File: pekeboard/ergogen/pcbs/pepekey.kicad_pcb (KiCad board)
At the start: 2 copper layers, 150.9 x 124.7 mm, 63 parts

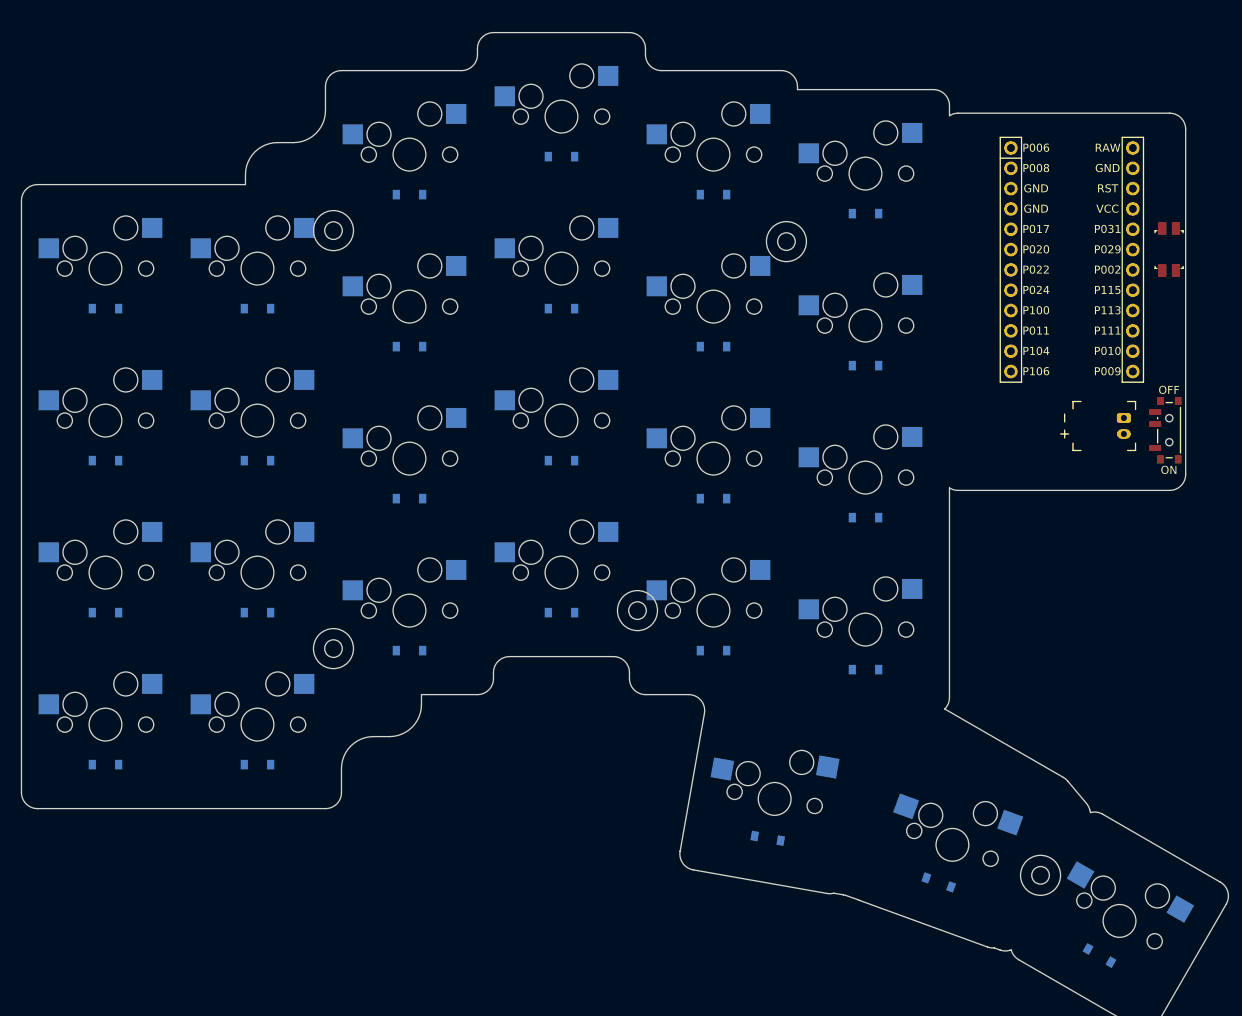
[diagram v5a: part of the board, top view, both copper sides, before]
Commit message: Adjusting mounting holes
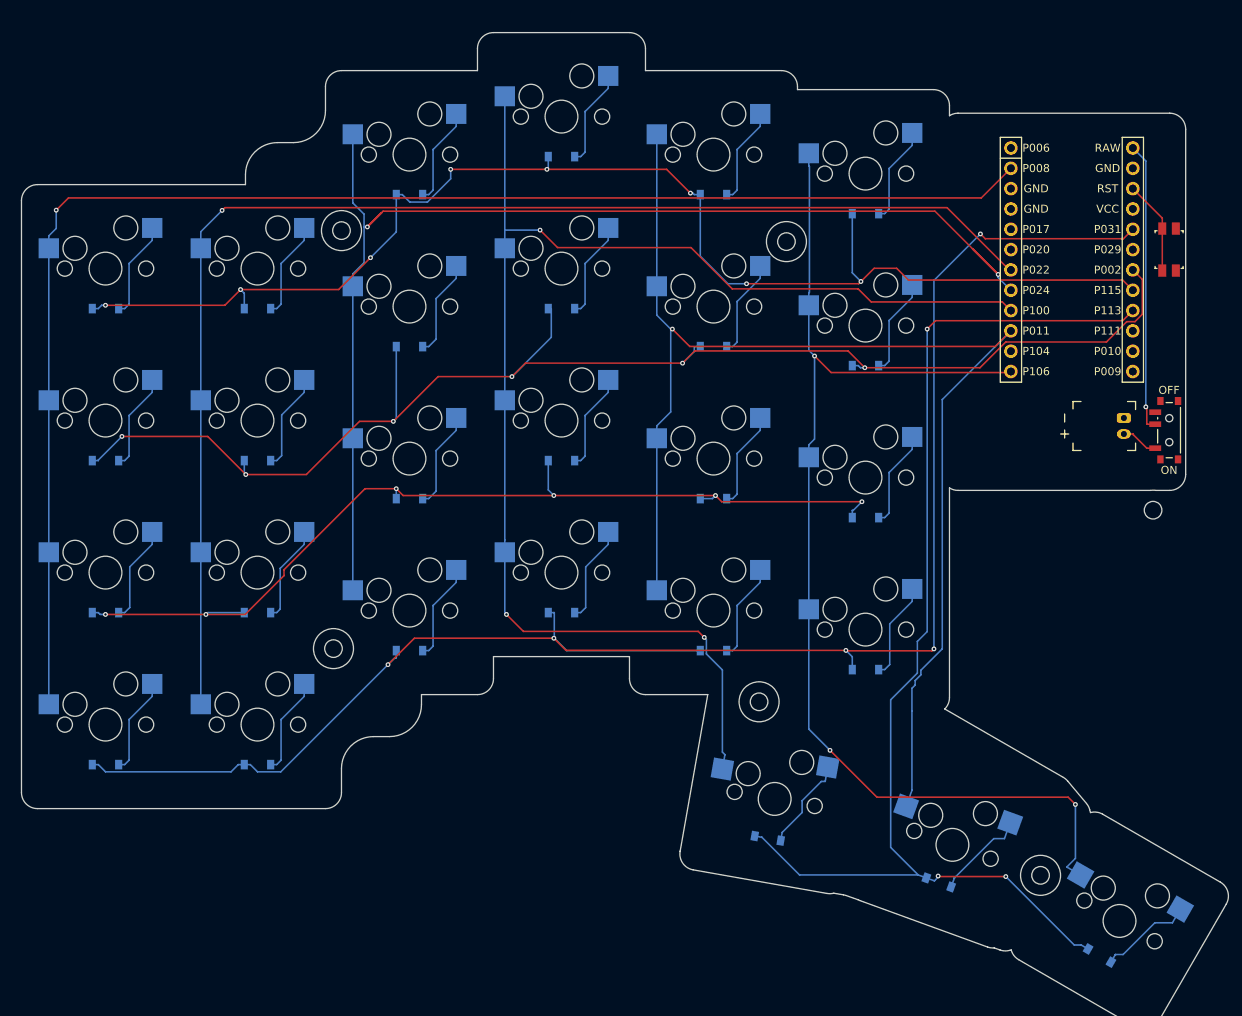
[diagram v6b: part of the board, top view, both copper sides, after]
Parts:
- added MH6: , ceoloide:mounting_hole_npth, F.Cu at (230.9, 93.2)
- moved MH4 19.0 mm to (181.7, 117.2)
- moved MH1 1.00 mm to (129.5, 58.2)
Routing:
- net P031: track 0.00 -> 216.0 mm, vias 0 -> 5
- net P008: track 0.00 -> 183.7 mm, vias 0 -> 1
- net P002: track 0.00 -> 177.9 mm, vias 0 -> 6
- net P100: track 0.00 -> 175.8 mm, vias 0 -> 3
- net P024: track 0.00 -> 172.3 mm, vias 0 -> 2
- net P011: track 0.00 -> 167.4 mm, vias 0 -> 1
- net P115: track 0.00 -> 167.0 mm, vias 0 -> 8
- net P022: track 0.00 -> 164.8 mm, vias 0 -> 1
- net P113: track 0.00 -> 146.0 mm, vias 0 -> 3
- net P106: track 0.00 -> 145.6 mm, vias 0 -> 3
- net P025: track 0.00 -> 119.3 mm, vias 0 -> 6
- net RAW: track 0.00 -> 36.3 mm, vias 0 -> 1
- net ring_num: track 0.00 -> 12.3 mm
- net inner_num: track 0.00 -> 12.3 mm
- net ring_bottom: track 0.00 -> 12.3 mm
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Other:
- outline, holes or cut-outs redrawn

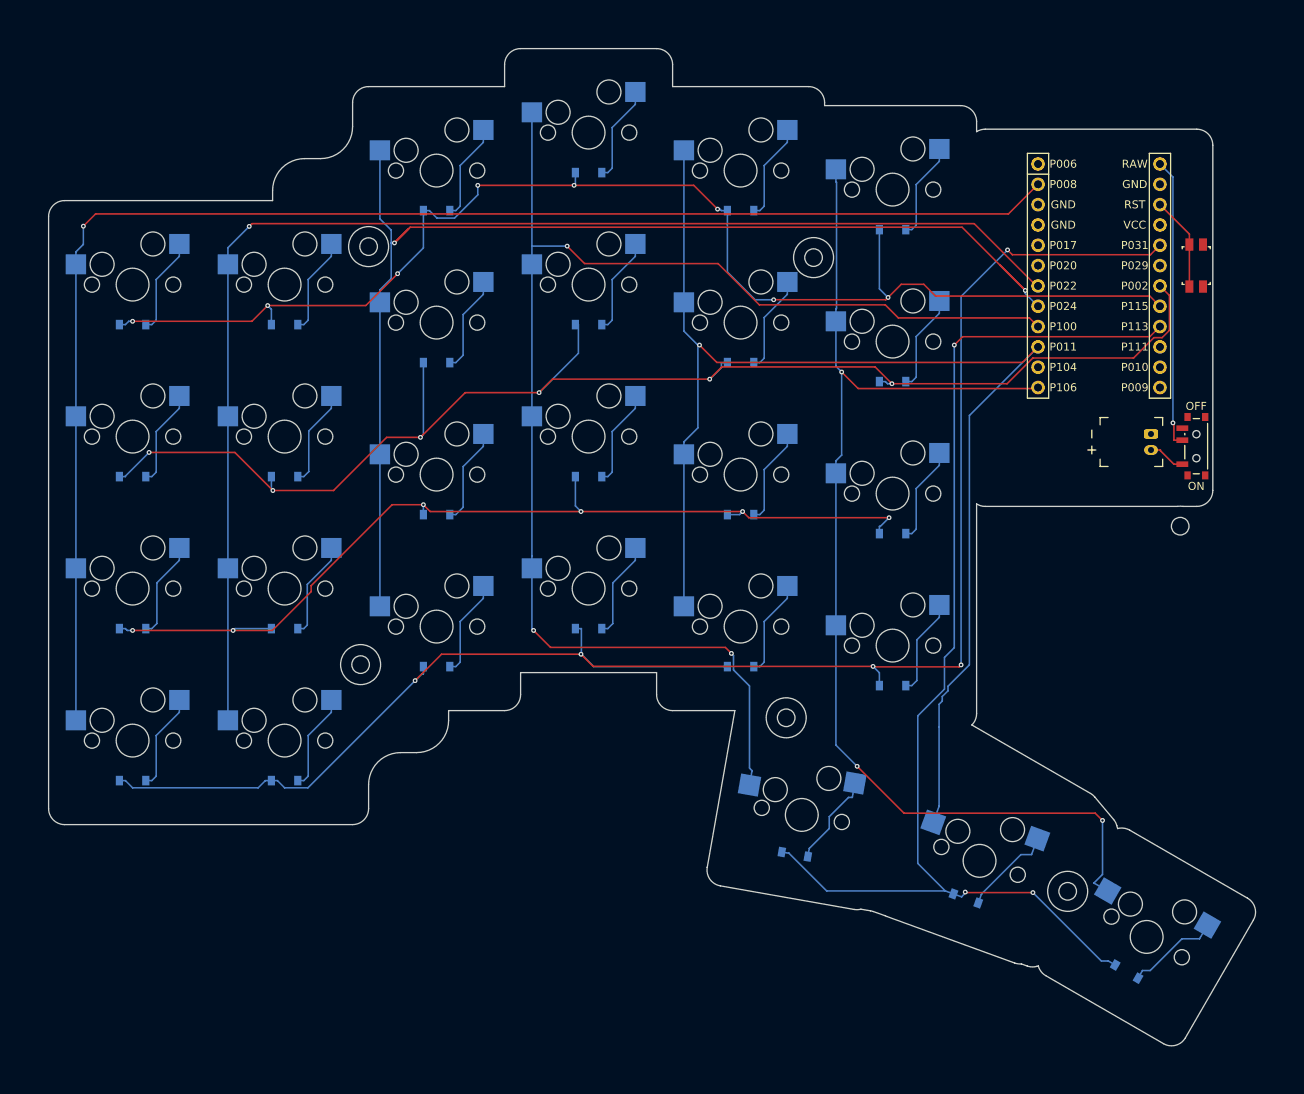
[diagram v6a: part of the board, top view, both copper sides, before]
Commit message: Fix mounting hole outside PCB
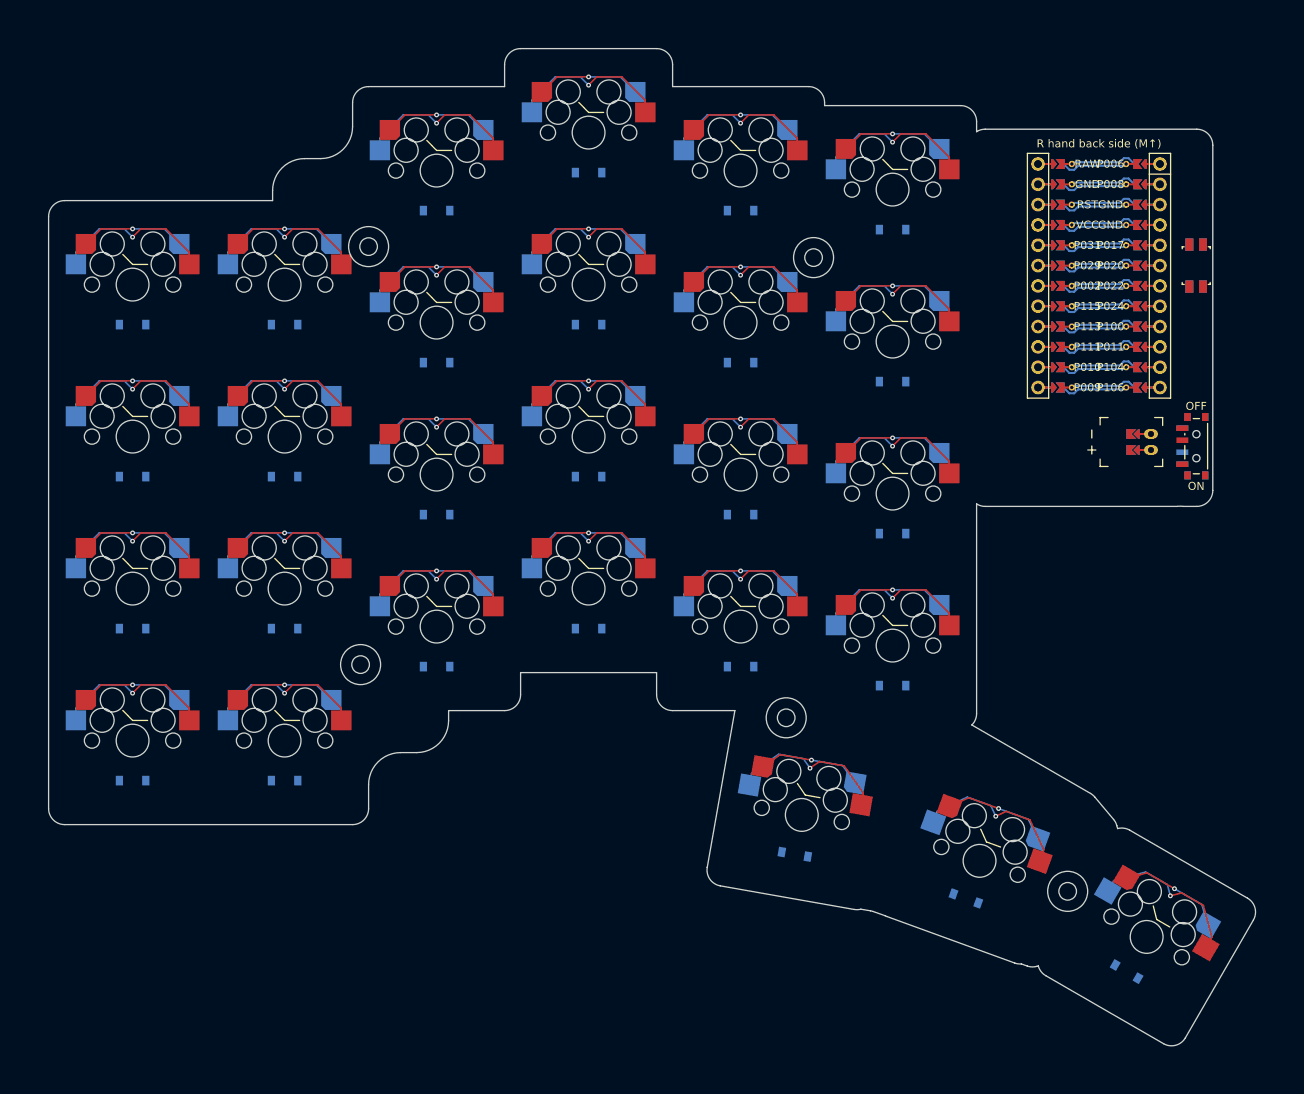
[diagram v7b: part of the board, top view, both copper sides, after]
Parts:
- removed MH6: , ceoloide:mounting_hole_npth
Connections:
- JST1 pad 1: GND -> BAT_P
- JST1 pad 2: BAT_P -> GND
- MCU1 pad 1: RAW -> MCU1_1
- MCU1 pad 10: P111 -> MCU1_10
- MCU1 pad 11: P010 -> MCU1_11
- MCU1 pad 12: P009 -> MCU1_12
- MCU1 pad 13: P106 -> MCU1_13
- MCU1 pad 14: P104 -> MCU1_14
- MCU1 pad 15: P011 -> MCU1_15
- MCU1 pad 16: P100 -> MCU1_16
- MCU1 pad 17: P024 -> MCU1_17
- MCU1 pad 18: P022 -> MCU1_18
- MCU1 pad 19: P020 -> MCU1_19
- MCU1 pad 2: GND -> MCU1_2
- MCU1 pad 20: P017 -> MCU1_20
- MCU1 pad 21: GND -> MCU1_21
- MCU1 pad 22: GND -> MCU1_22
- MCU1 pad 23: P008 -> MCU1_23
- MCU1 pad 24: P006 -> MCU1_24
- MCU1 pad 3: RST -> MCU1_3
- MCU1 pad 4: VCC -> MCU1_4
- MCU1 pad 5: P031 -> MCU1_5
- MCU1 pad 6: P029 -> MCU1_6
- MCU1 pad 7: P002 -> MCU1_7
- MCU1 pad 8: P115 -> MCU1_8
- MCU1 pad 9: P113 -> MCU1_9
- PWR1 pad 3: (no net) -> BAT_P
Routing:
- net (no net): track 0.00 -> 337.7 mm
- net P031: track 216.0 -> 0.00 mm, vias 5 -> 0
- net P002: track 177.9 -> 0.00 mm, vias 6 -> 0
- net P115: track 167.0 -> 0.00 mm, vias 8 -> 0
- net P113: track 146.0 -> 0.00 mm, vias 3 -> 0
- net P008: track 183.7 -> 42.3 mm, vias 1 -> 4
- net P024: track 172.3 -> 42.3 mm, vias 2 -> 4
- net P100: track 175.8 -> 52.9 mm, vias 3 -> 5
- net P022: track 164.8 -> 42.3 mm, vias 1 -> 4
- net P025: track 119.3 -> 0.00 mm, vias 6 -> 0
- net P011: track 167.4 -> 52.9 mm, vias 1 -> 5
- net P106: track 145.6 -> 52.9 mm, vias 3 -> 5
- net RAW: track 36.3 -> 0.00 mm, vias 1 -> 0
- net RST: track 11.8 -> 0.00 mm
- net middle_thumbrow: track 11.6 -> 23.1 mm, vias 0 -> 1
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
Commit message: reversible diodes removing fill zone
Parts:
- D1, D10, D11, D12, D13, D14, D15, D16, D17, D18, D19, D2, D20, D21, D22, D23, D24, D25, D26, D27, D3, D4, D5, D6, D7, D8, D9: moved to F.Cu
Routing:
- net (no net): track 337.7 -> 0.00 mm
- net P008: track 42.3 -> 268.6 mm
- net P031: track 0.00 -> 206.8 mm, vias 0 -> 6
- net P100: track 52.9 -> 258.8 mm, vias 5 -> 6
- net P011: track 52.9 -> 258.2 mm, vias 5 -> 6
- net P106: track 52.9 -> 251.5 mm, vias 5 -> 7
- net P022: track 42.3 -> 240.4 mm, vias 4 -> 5
- net P024: track 42.3 -> 230.4 mm
- net P115: track 0.00 -> 164.6 mm, vias 0 -> 6
- net P002: track 0.00 -> 158.9 mm, vias 0 -> 6
- net P113: track 0.00 -> 154.5 mm, vias 0 -> 3
- net P025: track 0.00 -> 120.0 mm, vias 0 -> 6
- net GND: track 0.00 -> 89.7 mm, vias 0 -> 2
- net RAW: track 0.00 -> 56.1 mm, vias 0 -> 1
- net RST: track 0.00 -> 47.5 mm
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- removed copper zone on F.Cu, net GND
